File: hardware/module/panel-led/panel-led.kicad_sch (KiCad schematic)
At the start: 2 parts

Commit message: WIP module schematics: footprints, bought-part fields, and the two board projects (module-main, module-jack)
Recovered from a container restart; not yet exported or checked.

Co-Authored-By: Claude Opus 5.5 <noreply@anthropic.com>
Claude-Session: https://claude.ai/code/session_01LmB4muFXnoLprWX4JzuJ5A
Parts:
- LED-PANEL: footprint (none) -> LED_THT:LED_D3.0mm; Assembly (none) -> hand; LCSC (none) -> C125082; MPN (none) -> LTL-4231N; Manufacturer (none) -> Lite-On
- R-LED-PANEL: footprint (none) -> Resistor_SMD:R_0805_2012Metric; Assembly (none) -> machine; LCSC (none) -> C17520; MPN (none) -> 0805W8F2201T5E; Manufacturer (none) -> UNI-ROYAL(Uniroyal Elec)
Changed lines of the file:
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@@
     (property "Reference" "R-LED-PANEL" (at 43.18 49.53 0) (effects (font (size 1.27 1.27)) (justify left)))
     (property "Value" "2k2 1%" (at 43.18 52.07 0) (effects (font (size 1.27 1.27)) (justify left)))
-    (property "Footprint" "" (at 39.37 50.8 0) (effects (font (size 1.27 1.27)) hide))
+    (property "Footprint" "Resistor_SMD:R_0805_2012Metric" (at 39.37 50.8 0) (effects (font (size 1.27 1.27)) hide))
     (property "Datasheet" "" (at 40.64 50.8 0) (effects (font (size 1.27 1.27)) hide))
     (property "Row" "R-LED-PANEL" (at 40.64 50.8 0) (effects (font (size 1.27 1.27)) hide))
     (property "Pins" "1=1 2=2" (at 40.64 50.8 0) (effects (font (size 1.27 1.27)) hide))
+    (property "Manufacturer" "UNI-ROYAL(Uniroyal Elec)" (at 40.64 50.8 0) (effects (font (size 1.27 1.27)) hide))
+    (property "MPN" "0805W8F2201T5E" (at 40.64 50.8 0) (effects (font (size 1.27 1.27)) hide))
+    (property "LCSC" "C17520" (at 40.64 50.8 0) (effects (font (size 1.27 1.27)) hide))
+    (property "Assembly" "machine" (at 40.64 50.8 0) (effects (font (size 1.27 1.27)) hide))
     (pin "1")
     (pin "2")
-    (instances (project "panel-led" (path "/5869b789-0aae-533b-a7bd-19d896fa22ed" (reference "R-LED-PANEL") (unit 1))))
+    (instances (project "module-jack" (path "/f69c67ba-c380-5393-90d5-6d2847e300fb/d1b77d3e-fc31-5614-a8a2-e593547fc87c" (reference "R1") (unit 1))) (project "panel-led" (path "/5869b789-0aae-533b-a7bd-19d896fa22ed" (reference "R-LED-PANEL") (unit 1))))
   )
   (symbol (lib_id "Device:LED") (at 91.44 50.8 0) (unit 1)
@@
     (property "Reference" "LED-PANEL" (at 91.44 48.26 0) (effects (font (size 1.27 1.27))))
     (property "Value" "3mm LED" (at 91.44 53.34 0) (effects (font (size 1.27 1.27))))
-    (property "Footprint" "" (at 91.44 50.8 0) (effects (font (size 1.27 1.27)) hide))
+    (property "Footprint" "LED_THT:LED_D3.0mm" (at 91.44 50.8 0) (effects (font (size 1.27 1.27)) hide))
     (property "Datasheet" "" (at 91.44 50.8 0) (effects (font (size 1.27 1.27)) hide))
     (property "Row" "LED-PANEL" (at 91.44 50.8 0) (effects (font (size 1.27 1.27)) hide))
@@
     (property "Note" "AN ORDINARY POWER INDICATOR NOW. It was kept to show the presence comparator's collector node, and that comparator is not fitted - so it says the rack is on and nothing else. It is live whenever the rack is, which is the whole of the page's open item" (at 91.44 50.8 0) (effects (font (size 1.27 1.27)) hide))
     (property "Pins_source" "datasheets/led/LITEON-LTL-4231N-3MM-GREEN-DIFFUSED.pdf: the short lead and the flat are the cathode; KiCad's LED_D3.0mm pad 1 is the cathode" (at 91.44 50.8 0) (effects (font (size 1.27 1.27)) hide))
+    (property "Manufacturer" "Lite-On" (at 91.44 50.8 0) (effects (font (size 1.27 1.27)) hide))
+    (property "MPN" "LTL-4231N" (at 91.44 50.8 0) (effects (font (size 1.27 1.27)) hide))
+    (property "LCSC" "C125082" (at 91.44 50.8 0) (effects (font (size 1.27 1.27)) hide))
+    (property "Assembly" "hand" (at 91.44 50.8 0) (effects (font (size 1.27 1.27)) hide))
     (pin "1")
     (pin "2")
-    (instances (project "panel-led" (path "/5869b789-0aae-533b-a7bd-19d896fa22ed" (reference "LED-PANEL") (unit 1))))
+    (instances (project "module-jack" (path "/f69c67ba-c380-5393-90d5-6d2847e300fb/d1b77d3e-fc31-5614-a8a2-e593547fc87c" (reference "D1") (unit 1))) (project "panel-led" (path "/5869b789-0aae-533b-a7bd-19d896fa22ed" (reference "LED-PANEL") (unit 1))))
   )
   (wire (pts (xy 40.64 46.99) (xy 40.64 44.45)) (stroke (width 0) (type default)))

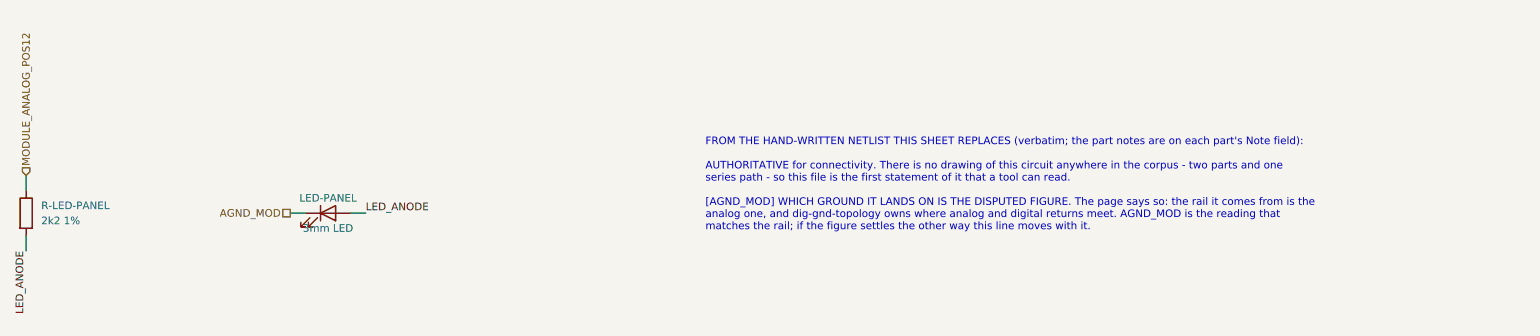
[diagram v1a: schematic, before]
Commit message: Panel LED hangs on the load switch output: lit = delivering, dark = off or latched
The LED was on the analog +12 V rail, live whenever the rack is, so it could
not show the -1's latch - the one thing it was kept for. The banked LT1641
datasheet shows TIMER and GATE hold no 'latched' level and PWRGD has the wrong
sense; the output does. J-B2B-MOD pin 19 carries UMBILICAL_POS12 on both
boards; nets.yaml and the allocation table follow.

Co-Authored-By: Claude Opus 5.5 <noreply@anthropic.com>
Claude-Session: https://claude.ai/code/session_01LmB4muFXnoLprWX4JzuJ5A
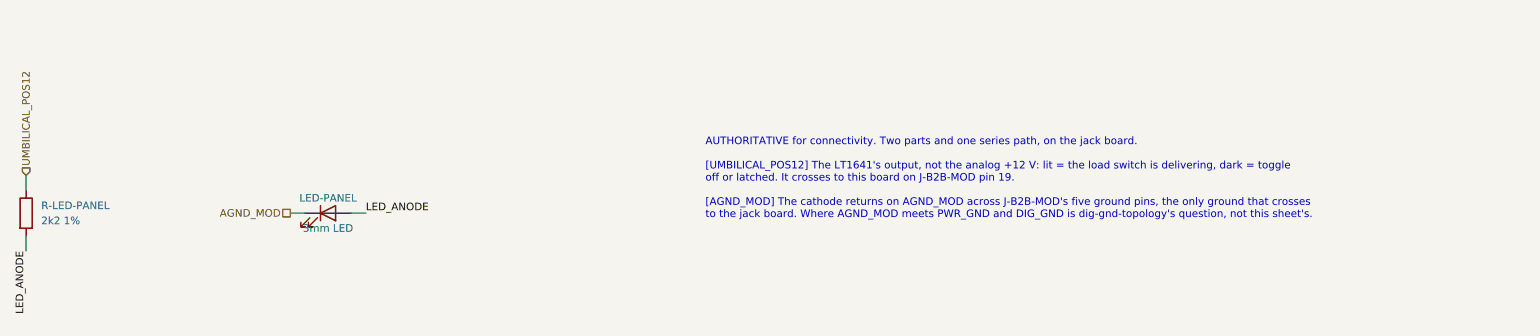
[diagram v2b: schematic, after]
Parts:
- LED-PANEL: Note AN ORDINARY POWER INDICATOR NOW. It was kept to show the pr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 -> LIT = THE LOAD SWITCH IS DELIVERING. It hangs on UMBILICAL_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
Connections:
- net MODULE_ANALOG_POS12 renamed UMBILICAL_POS12
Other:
- note added: "AUTHORITATIVE for connectivity. Two parts and one series path, on the jack board. [UMBILICAL_POS12] The LT1641's output, not the analog +12 V: lit = the load switch is delivering, dark = toggle off or latched. It crosses to this board on J-B2B-MOD pin 19. [AGND_MOD] The cathode returns on AGND_MOD across J-B2B-MOD's five ground pins, the only ground that crosses to the jack board. Where AGND_MOD 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"
- note removed: "FROM THE HAND-WRITTEN NETLIST THIS SHEET REPLACES (verbatim; the part notes are on each part's Note field): AUTHORITATIVE for connectivity. There is no drawing of this circuit anywhere in the corpus - two parts and one series path - so this file is the first statement of it that a tool can read. [AGND_MOD] WHICH GROUND IT LANDS ON IS THE DISPUTED FIGURE. The page says so: the rail it comes from i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"
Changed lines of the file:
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@@
     (property "Row" "LED-PANEL" (at 91.44 50.8 0) (effects (font (size 1.27 1.27)) hide))
     (property "Pins" "A=2(A) K=1(K)" (at 91.44 50.8 0) (effects (font (size 1.27 1.27)) hide))
-    (property "Note" "AN ORDINARY POWER INDICATOR NOW. It was kept to show the presence comparator's collector node, and that comparator is not fitted - so it says the rack is on and nothing else. It is live whenever the rack is, which is the whole of the page's open item" (at 91.44 50.8 0) (effects (font (size 1.27 1.27)) hide))
+    (property "Note" "LIT = THE LOAD SWITCH IS DELIVERING. It hangs on UMBILICAL_POS12, the LT1641 output, so it is dark with the toggle off and dark when the -1 has latched on a fault - the one indication the latching design needs. It does not say the instrument is plugged in" (at 91.44 50.8 0) (effects (font (size 1.27 1.27)) hide))
     (property "Pins_source" "datasheets/led/LITEON-LTL-4231N-3MM-GREEN-DIFFUSED.pdf: the short lead and the flat are the cathode; KiCad's LED_D3.0mm pad 1 is the cathode" (at 91.44 50.8 0) (effects (font (size 1.27 1.27)) hide))
     (property "Manufacturer" "Lite-On" (at 91.44 50.8 0) (effects (font (size 1.27 1.27)) hide))
@@
   )
   (wire (pts (xy 40.64 46.99) (xy 40.64 44.45)) (stroke (width 0) (type default)))
-  (hierarchical_label "MODULE_ANALOG_POS12" (shape input) (at 40.64 44.45 90) (effects (font (size 1.27 1.27)) (justify left))
+  (hierarchical_label "UMBILICAL_POS12" (shape input) (at 40.64 44.45 90) (effects (font (size 1.27 1.27)) (justify left))
     (property "Dir" "in" (at 40.64 44.45 0) (effects (font (size 1.27 1.27)) hide))
-    (property "From" "module/power-entry" (at 40.64 44.45 0) (effects (font (size 1.27 1.27)) hide)))
+    (property "From" "module/umbilical-load-switch" (at 40.64 44.45 0) (effects (font (size 1.27 1.27)) hide))
+    (property "Figure" "umbilical-current" (at 40.64 44.45 0) (effects (font (size 1.27 1.27)) hide)))
   (wire (pts (xy 40.64 54.61) (xy 40.64 57.15)) (stroke (width 0) (type default)))
   (label "LED_ANODE" (at 40.64 57.15 270) (fields_autoplaced) (effects (font (size 1.27 1.27)) (justify right bottom)))
@@
     (property "From" "module/power-entry" (at 85.09 50.8 0) (effects (font (size 1.27 1.27)) hide))
     (property "Figure" "dig-gnd-topology" (at 85.09 50.8 0) (effects (font (size 1.27 1.27)) hide)))
-  (text "FROM THE HAND-WRITTEN NETLIST THIS SHEET REPLACES (verbatim; the part notes are on each part's Note field):\n\nAUTHORITATIVE for connectivity. There is no drawing of this circuit anywhere in the corpus - two parts and one\nseries path - so this file is the first statement of it that a tool can read.\n\n[AGND_MOD] WHICH GROUND IT LANDS ON IS THE DISPUTED FIGURE. The page says so: the rail it comes from is the\nanalog one, and dig-gnd-topology owns where analog and digital returns meet. AGND_MOD is the reading that\nmatches the rail; if the figure settles the other way this line moves with it." (at 154.94 38.099999999999994 0) (effects (font (size 1.27 1.27)) (justify left top)))
+  (text "AUTHORITATIVE for connectivity. Two parts and one series path, on the jack board.\n\n[UMBILICAL_POS12] The LT1641's output, not the analog +12 V: lit = the load switch is delivering, dark = toggle\noff or latched. It crosses to this board on J-B2B-MOD pin 19.\n\n[AGND_MOD] The cathode returns on AGND_MOD across J-B2B-MOD's five ground pins, the only ground that crosses\nto the jack board. Where AGND_MOD meets PWR_GND and DIG_GND is dig-gnd-topology's question, not this sheet's." (at 154.94 38.099999999999994 0) (effects (font (size 1.27 1.27)) (justify left top)))
   (sheet_instances (path "/" (page "1")))
 )

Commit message: LED-PANEL moves to the main board (LTST-C171GKT under a Bivar PLP2-750 light pipe); J-B2B-MOD pin 19 freed; jack board keeps H1-H2; panel standoffs and studs in the BOM
Co-Authored-By: Claude Opus 5.5 <noreply@anthropic.com>
Claude-Session: https://claude.ai/code/session_01LmB4muFXnoLprWX4JzuJ5A
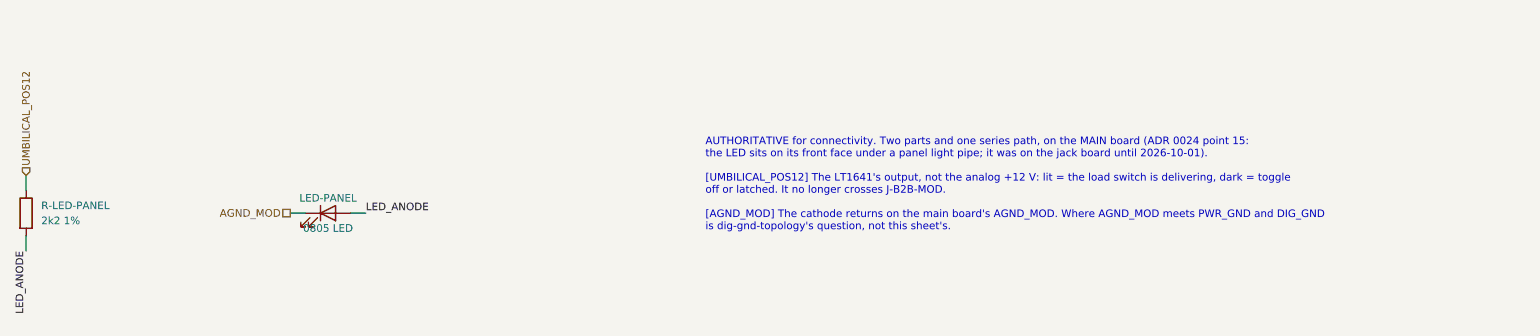
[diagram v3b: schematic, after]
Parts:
- LED-PANEL: value 3mm LED -> 0805 LED; footprint LED_THT:LED_D3.0mm -> LED_SMD:LED_0805_2012Metric; Assembly hand -> machine; LCSC C125082 -> C913075; MPN LTL-4231N -> LTST-C171GKT; Note LIT = THE LOAD SWITCH IS DELIVERING. It hangs on UMBILICAL_POS12, the LT1641 output, so it is dark with the toggle off and dark when the -1 has latched on a fault - the one indication the latching design needs. It does not say the instrument is plugged in -> LIT = THE LOAD SWITCH IS DELIVERING. It hangs on UMBILICAL_POS12, the LT1641 output, so it is dark with the toggle off and dark when the -1 has latched on a fault - the one indication the latching design needs. It does not say the instrument is plugged in. On the MAIN board's front face, under MECH-LED-BEZEL-MOD, the panel light pipe (ADR 0024 point 15); Pins_source datasheets/led/LITEON-LTL-4231N-3MM-GREEN-DIFFUSED.pdf: the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 -> datasheets/led/LITEON-LTST-C171GKT-0805-GREEN.pdf p.1: the 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
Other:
- note added: "AUTHORITATIVE for connectivity. Two parts and one series path, on the MAIN board (ADR 0024 point 15: the LED sits on its front face under a panel light pipe; it was on the jack board until 2026-10-01). [UMBILICAL_POS12] The LT1641's output, not the analog +12 V: lit = the load switch is delivering, dark = toggle off or latched. It no longer crosses J-B2B-MOD. [AGND_MOD] The cathode returns on the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"
- note removed: "AUTHORITATIVE for connectivity. Two parts and one series path, on the jack board. [UMBILICAL_POS12] The LT1641's output, not the analog +12 V: lit = the load switch is delivering, dark = toggle off or latched. It crosses to this board on J-B2B-MOD pin 19. [AGND_MOD] The cathode returns on AGND_MOD across J-B2B-MOD's five ground pins, the only ground that crosses to the jack board. Where AGND_MOD 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"
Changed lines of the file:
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@@
     (pin "1")
     (pin "2")
-    (instances (project "module-jack" (path "/f69c67ba-c380-5393-90d5-6d2847e300fb/d1b77d3e-fc31-5614-a8a2-e593547fc87c" (reference "R1") (unit 1))) (project "panel-led" (path "/5869b789-0aae-533b-a7bd-19d896fa22ed" (reference "R-LED-PANEL") (unit 1))))
+    (instances (project "module-main" (path "/fc77e9f9-9171-5c83-92ae-8cafe880764e/00556410-138e-4c9b-bcc3-1c0a26b76f50" (reference "R71") (unit 1))) (project "panel-led" (path "/5869b789-0aae-533b-a7bd-19d896fa22ed" (reference "R-LED-PANEL") (unit 1))))
   )
   (symbol (lib_id "Device:LED") (at 91.44 50.8 0) (unit 1)
     (in_bom yes) (on_board yes) (dnp no)
     (property "Reference" "LED-PANEL" (at 91.44 48.26 0) (effects (font (size 1.27 1.27))))
-    (property "Value" "3mm LED" (at 91.44 53.34 0) (effects (font (size 1.27 1.27))))
-    (property "Footprint" "LED_THT:LED_D3.0mm" (at 91.44 50.8 0) (effects (font (size 1.27 1.27)) hide))
+    (property "Value" "0805 LED" (at 91.44 53.34 0) (effects (font (size 1.27 1.27))))
+    (property "Footprint" "LED_SMD:LED_0805_2012Metric" (at 91.44 50.8 0) (effects (font (size 1.27 1.27)) hide))
     (property "Datasheet" "" (at 91.44 50.8 0) (effects (font (size 1.27 1.27)) hide))
     (property "Row" "LED-PANEL" (at 91.44 50.8 0) (effects (font (size 1.27 1.27)) hide))
     (property "Pins" "A=2(A) K=1(K)" (at 91.44 50.8 0) (effects (font (size 1.27 1.27)) hide))
-    (property "Note" "LIT = THE LOAD SWITCH IS DELIVERING. It hangs on UMBILICAL_POS12, the LT1641 output, so it is dark with the toggle off and dark when the -1 has latched on a fault - the one indication the latching design needs. It does not say the instrument is plugged in" (at 91.44 50.8 0) (effects (font (size 1.27 1.27)) hide))
-    (property "Pins_source" "datasheets/led/LITEON-LTL-4231N-3MM-GREEN-DIFFUSED.pdf: the short lead and the flat are the cathode; KiCad's LED_D3.0mm pad 1 is the cathode" (at 91.44 50.8 0) (effects (font (size 1.27 1.27)) hide))
+    (property "Note" "LIT = THE LOAD SWITCH IS DELIVERING. It hangs on UMBILICAL_POS12, the LT1641 output, so it is dark with the toggle off and dark when the -1 has latched on a fault - the one indication the latching design needs. It does not say the instrument is plugged in. On the MAIN board's front face, under MECH-LED-BEZEL-MOD, the panel light pipe (ADR 0024 point 15)" (at 91.44 50.8 0) (effects (font (size 1.27 1.27)) hide))
+    (property "Pins_source" "datasheets/led/LITEON-LTST-C171GKT-0805-GREEN.pdf p.1: the cathode is the end the package drawing marks CATHODE (the polarity bar); KiCad's LED_0805_2012Metric pad 1 is the cathode" (at 91.44 50.8 0) (effects (font (size 1.27 1.27)) hide))
     (property "Manufacturer" "Lite-On" (at 91.44 50.8 0) (effects (font (size 1.27 1.27)) hide))
-    (property "MPN" "LTL-4231N" (at 91.44 50.8 0) (effects (font (size 1.27 1.27)) hide))
-    (property "LCSC" "C125082" (at 91.44 50.8 0) (effects (font (size 1.27 1.27)) hide))
-    (property "Assembly" "hand" (at 91.44 50.8 0) (effects (font (size 1.27 1.27)) hide))
+    (property "MPN" "LTST-C171GKT" (at 91.44 50.8 0) (effects (font (size 1.27 1.27)) hide))
+    (property "LCSC" "C913075" (at 91.44 50.8 0) (effects (font (size 1.27 1.27)) hide))
+    (property "Assembly" "machine" (at 91.44 50.8 0) (effects (font (size 1.27 1.27)) hide))
     (pin "1")
     (pin "2")
-    (instances (project "module-jack" (path "/f69c67ba-c380-5393-90d5-6d2847e300fb/d1b77d3e-fc31-5614-a8a2-e593547fc87c" (reference "D1") (unit 1))) (project "panel-led" (path "/5869b789-0aae-533b-a7bd-19d896fa22ed" (reference "LED-PANEL") (unit 1))))
+    (instances (project "module-main" (path "/fc77e9f9-9171-5c83-92ae-8cafe880764e/00556410-138e-4c9b-bcc3-1c0a26b76f50" (reference "D16") (unit 1))) (project "panel-led" (path "/5869b789-0aae-533b-a7bd-19d896fa22ed" (reference "LED-PANEL") (unit 1))))
   )
   (wire (pts (xy 40.64 46.99) (xy 40.64 44.45)) (stroke (width 0) (type default)))
@@
     (property "From" "module/power-entry" (at 85.09 50.8 0) (effects (font (size 1.27 1.27)) hide))
     (property "Figure" "dig-gnd-topology" (at 85.09 50.8 0) (effects (font (size 1.27 1.27)) hide)))
-  (text "AUTHORITATIVE for connectivity. Two parts and one series path, on the jack board.\n\n[UMBILICAL_POS12] The LT1641's output, not the analog +12 V: lit = the load switch is delivering, dark = toggle\noff or latched. It crosses to this board on J-B2B-MOD pin 19.\n\n[AGND_MOD] The cathode returns on AGND_MOD across J-B2B-MOD's five ground pins, the only ground that crosses\nto the jack board. Where AGND_MOD meets PWR_GND and DIG_GND is dig-gnd-topology's question, not this sheet's." (at 154.94 38.099999999999994 0) (effects (font (size 1.27 1.27)) (justify left top)))
+  (text "AUTHORITATIVE for connectivity. Two parts and one series path, on the MAIN board (ADR 0024 point 15:\nthe LED sits on its front face under a panel light pipe; it was on the jack board until 2026-10-01).\n\n[UMBILICAL_POS12] The LT1641's output, not the analog +12 V: lit = the load switch is delivering, dark = toggle\noff or latched. It no longer crosses J-B2B-MOD.\n\n[AGND_MOD] The cathode returns on the main board's AGND_MOD. Where AGND_MOD meets PWR_GND and DIG_GND\nis dig-gnd-topology's question, not this sheet's." (at 154.94 38.099999999999994 0) (effects (font (size 1.27 1.27)) (justify left top)))
   (sheet_instances (path "/" (page "1")))
 )
